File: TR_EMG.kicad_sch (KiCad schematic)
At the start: 7 parts, among them J1 1727230, J2 1844236, J3 1727230, J4 MJ-3523-SMT-TR, J5 MJ-3523-SMT-TR, J6 MJ-3523-SMT-TR, J7 MJ-3523-SMT-TR

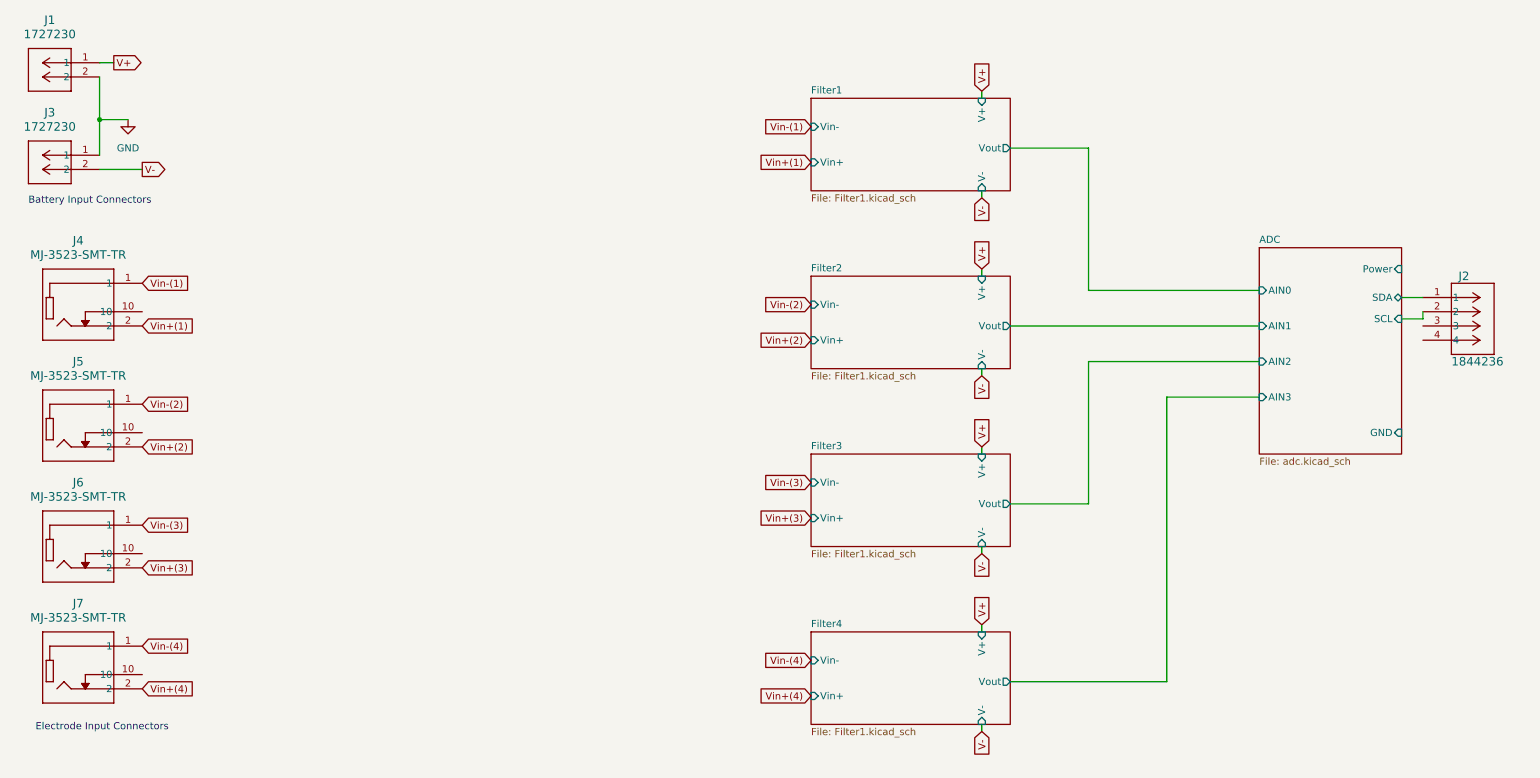
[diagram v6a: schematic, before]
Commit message: Reference Designator and Footprint Updates
Changed almost all reference designators to group similar components by what filter they are a part of and what value they have.

Need to:
- Sort symbol data for ADC and OpAmps to correct folders
- get footprint files for ADC and OpAmps
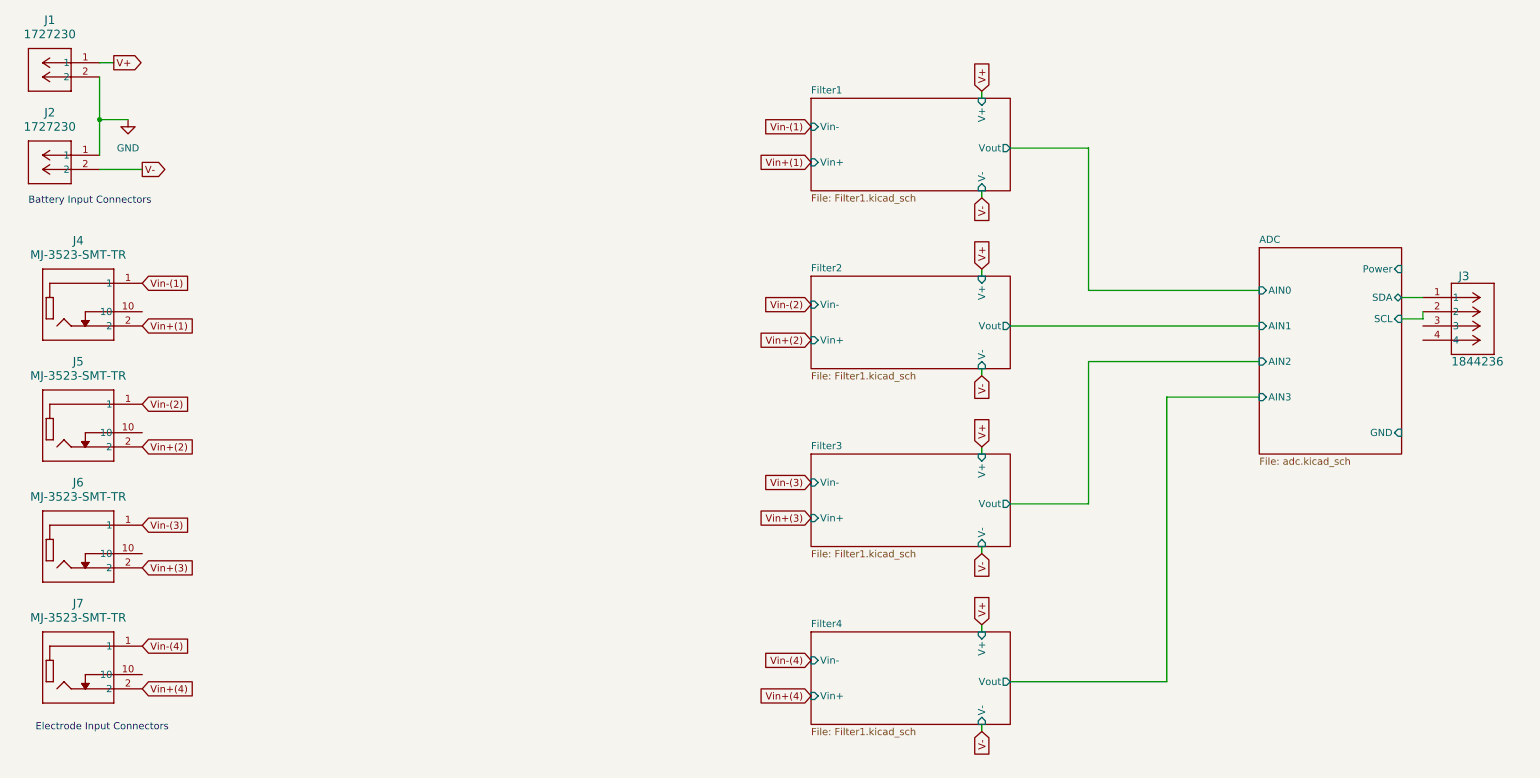
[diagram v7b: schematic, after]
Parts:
- J1: footprint CONN_1727230_PXC -> footprints:CONN_1727230_PXC
- J2: renamed from J3; footprint CONN_1727230_PXC -> footprints:CONN_1727230_PXC
- J3: renamed from J2; footprint CONN_1844236_PXC -> footprints:CONN_1844236_PXC
- J4, J5, J6, J7: footprint CONN_MJ-3523_CUD -> footprints:CONN_MJ-3523_CUD
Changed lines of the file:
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@@
       (effects (font (size 1.524 1.524)))
     )
-    (property "Footprint" "CONN_MJ-3523_CUD" (at 38.1 85.09 0)
+    (property "Footprint" "footprints:CONN_MJ-3523_CUD" (at 38.1 85.09 0)
       (effects (font (size 1.27 1.27) italic) hide)
     )
@@
   (symbol (lib_id "1727230:1727230") (at 30.48 40.64 0) (mirror y) (unit 1)
     (in_bom yes) (on_board yes) (dnp no) (fields_autoplaced)
-    (property "Reference" "J3" (at 21.59 33.02 0)
+    (property "Reference" "J2" (at 21.59 33.02 0)
       (effects (font (size 1.524 1.524)))
     )
@@
       (effects (font (size 1.524 1.524)))
     )
-    (property "Footprint" "CONN_1727230_PXC" (at 30.48 40.64 0)
+    (property "Footprint" "footprints:CONN_1727230_PXC" (at 30.48 40.64 0)
       (effects (font (size 1.27 1.27) italic) hide)
     )
@@
       (project "TR_EMG"
         (path "/c6167f6f-8a8c-40a1-9c06-7f0e8ea44639"
-          (reference "J3") (unit 1)
+          (reference "J2") (unit 1)
         )
       )
@@
       (effects (font (size 1.524 1.524)))
     )
-    (property "Footprint" "CONN_MJ-3523_CUD" (at 38.1 106.68 0)
+    (property "Footprint" "footprints:CONN_MJ-3523_CUD" (at 38.1 106.68 0)
       (effects (font (size 1.27 1.27) italic) hide)
     )
@@
       (effects (font (size 1.524 1.524)))
     )
-    (property "Footprint" "CONN_MJ-3523_CUD" (at 38.1 63.5 0)
+    (property "Footprint" "footprints:CONN_MJ-3523_CUD" (at 38.1 63.5 0)
       (effects (font (size 1.27 1.27) italic) hide)
     )
@@
       (effects (font (size 1.524 1.524)))
     )
-    (property "Footprint" "CONN_1727230_PXC" (at 30.48 24.13 0)
+    (property "Footprint" "footprints:CONN_1727230_PXC" (at 30.48 24.13 0)
       (effects (font (size 1.27 1.27) italic) hide)
     )
@@
   (symbol (lib_id "1844236:1844236") (at 266.7 66.04 0) (unit 1)
     (in_bom yes) (on_board yes) (dnp no)
-    (property "Reference" "J2" (at 273.05 62.23 0)
+    (property "Reference" "J3" (at 273.05 62.23 0)
       (effects (font (size 1.524 1.524)) (justify left))
     )
@@
       (effects (font (size 1.524 1.524)) (justify left))
     )
-    (property "Footprint" "CONN_1844236_PXC" (at 266.7 66.04 0)
+    (property "Footprint" "footprints:CONN_1844236_PXC" (at 266.7 66.04 0)
       (effects (font (size 1.27 1.27) italic) hide)
     )
@@
       (project "TR_EMG"
         (path "/c6167f6f-8a8c-40a1-9c06-7f0e8ea44639"
-          (reference "J2") (unit 1)
+          (reference "J3") (unit 1)
         )
       )
@@
       (effects (font (size 1.524 1.524)))
     )
-    (property "Footprint" "CONN_MJ-3523_CUD" (at 38.1 128.27 0)
+    (property "Footprint" "footprints:CONN_MJ-3523_CUD" (at 38.1 128.27 0)
       (effects (font (size 1.27 1.27) italic) hide)
     )

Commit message: updated GND symbols for appropriate seperatiion of analog and digital grounds
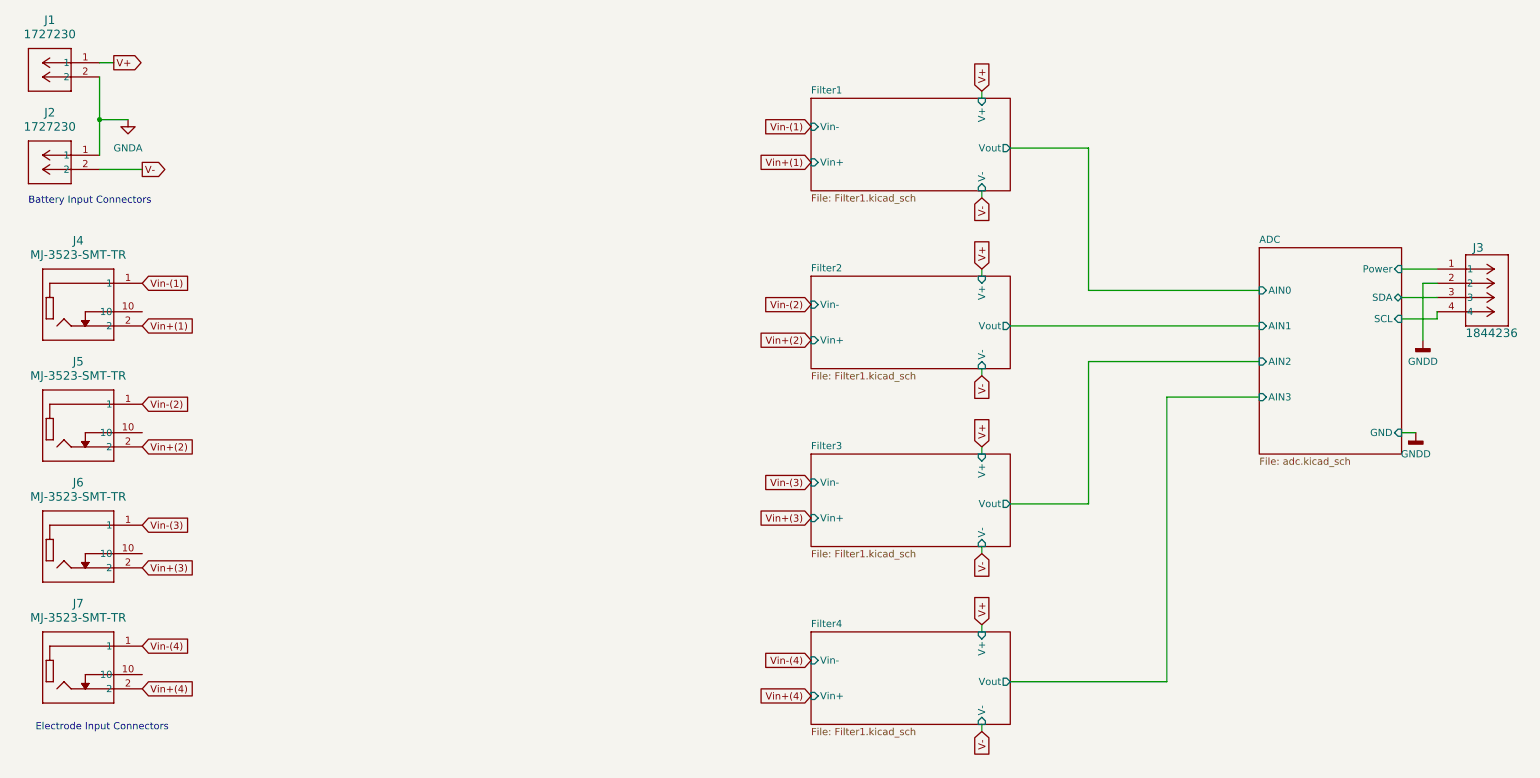
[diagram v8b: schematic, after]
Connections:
- net ADC/Power: now also J3.1
- net ADC/SCL: now also J3.4; no longer J3.2
- net ADC/SDA: now also J3.3; no longer J3.1
- net GND renamed GNDA
- new net GNDD: J3.2
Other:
- moved on the sheet: J3
